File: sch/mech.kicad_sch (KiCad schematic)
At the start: 15 parts, among them J12 Conn_01x03_Male, J3 ESD_strip_bottom, K1 Key_K1_K2_TE_1-1469373-1, K2 Key_K1_K2_TE_1-1469373-1

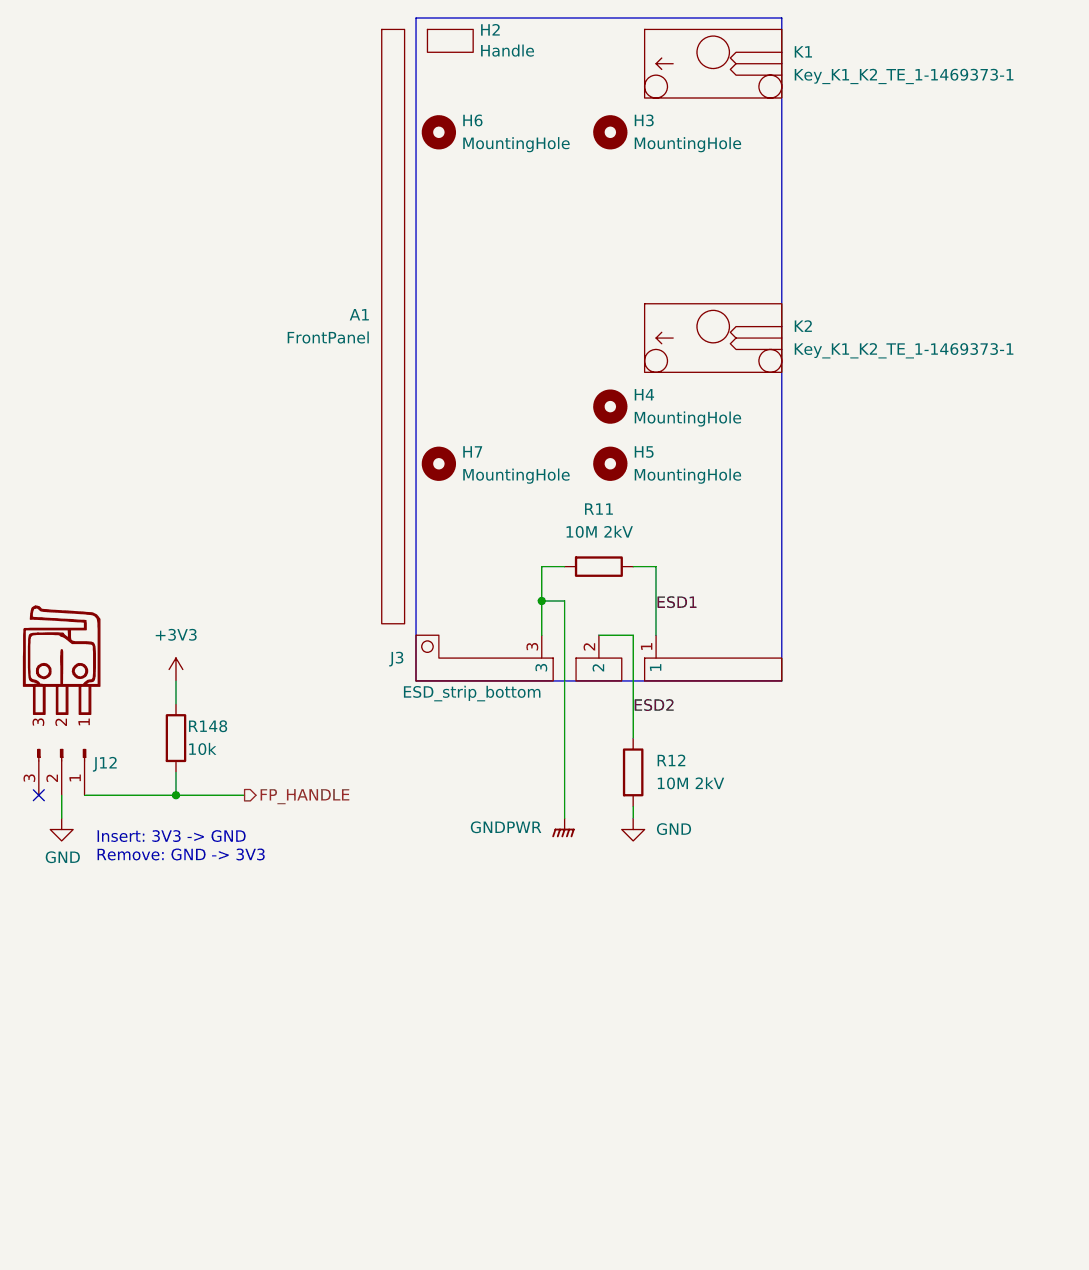
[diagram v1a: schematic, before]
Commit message: added fidutials
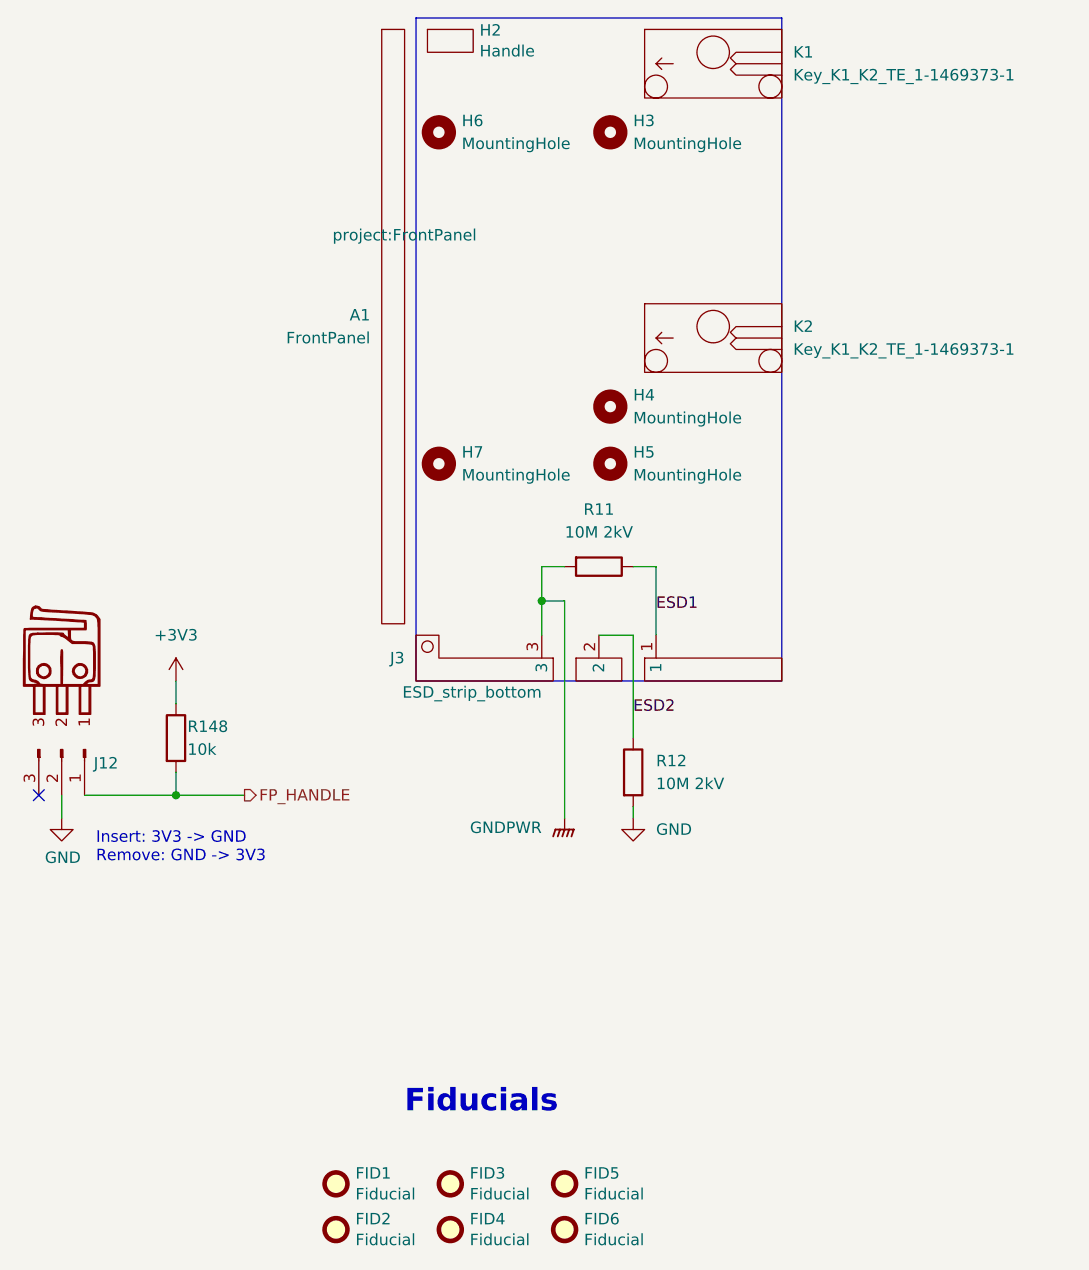
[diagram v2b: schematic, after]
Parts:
- added FID1, FID2, FID3, FID4, FID5, FID6: Fiducial, Fiducial:Fiducial_1mm_Mask2mm, symbol Mechanical:Fiducial
- A1: footprint KIT_Mechanical:FrontPanel -> project:FrontPanel
- H1: footprint KIT_Mechanical:81-301-00 -> project:81-301-00
- J12: footprint KIT_Connector:Molex_53046-0310 -> project:Molex_53046-0310
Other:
- note added: "Fiducials"
